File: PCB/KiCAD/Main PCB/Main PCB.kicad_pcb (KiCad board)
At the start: 2 copper layers, 118 x 118 mm, 145 parts, among them IC1 ADG608BRZ, IC2 ADG608BRZ, IC3 XB3-24Z8CM, J1 Conn_01x02, J2 Conn_01x02, J3 Conn_01x02, J4 Conn_Coaxial_Small, J5 Conn_01x02, J6 Conn_01x04, J7 Conn_01x04, J8 Conn_01x04, M1 Conn_01x02_Pin, M2 Conn_01x02_Pin, M3 Conn_01x02_Pin, M4 Conn_01x02_Pin, Q1 BSS138, Q2 BSS138, U2 Teensy4.1, U3 Teensy4.0, U4 LMD18200, U5 LMD18200, U6 LMD18200, U7 LMD18200, U8 MIC5219-3.3YM5

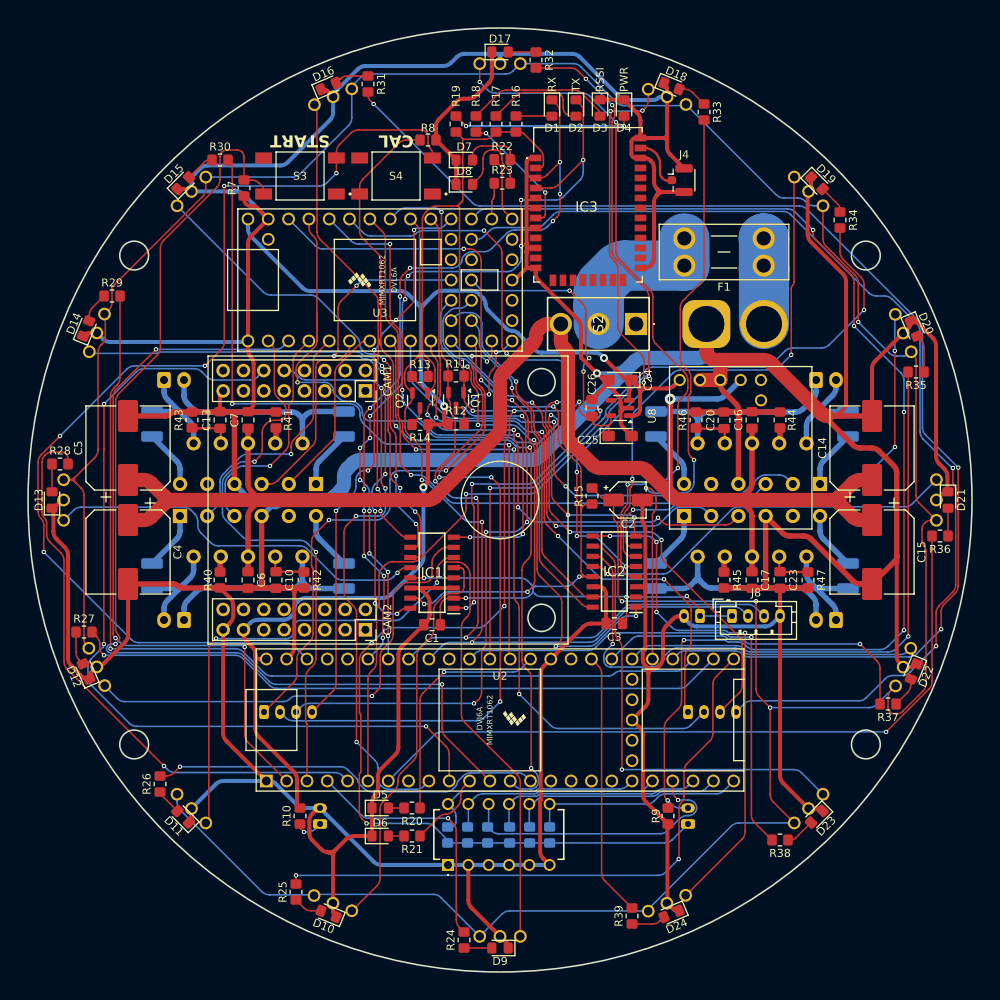
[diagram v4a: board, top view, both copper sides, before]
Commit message: New motor controllers for the main PCB
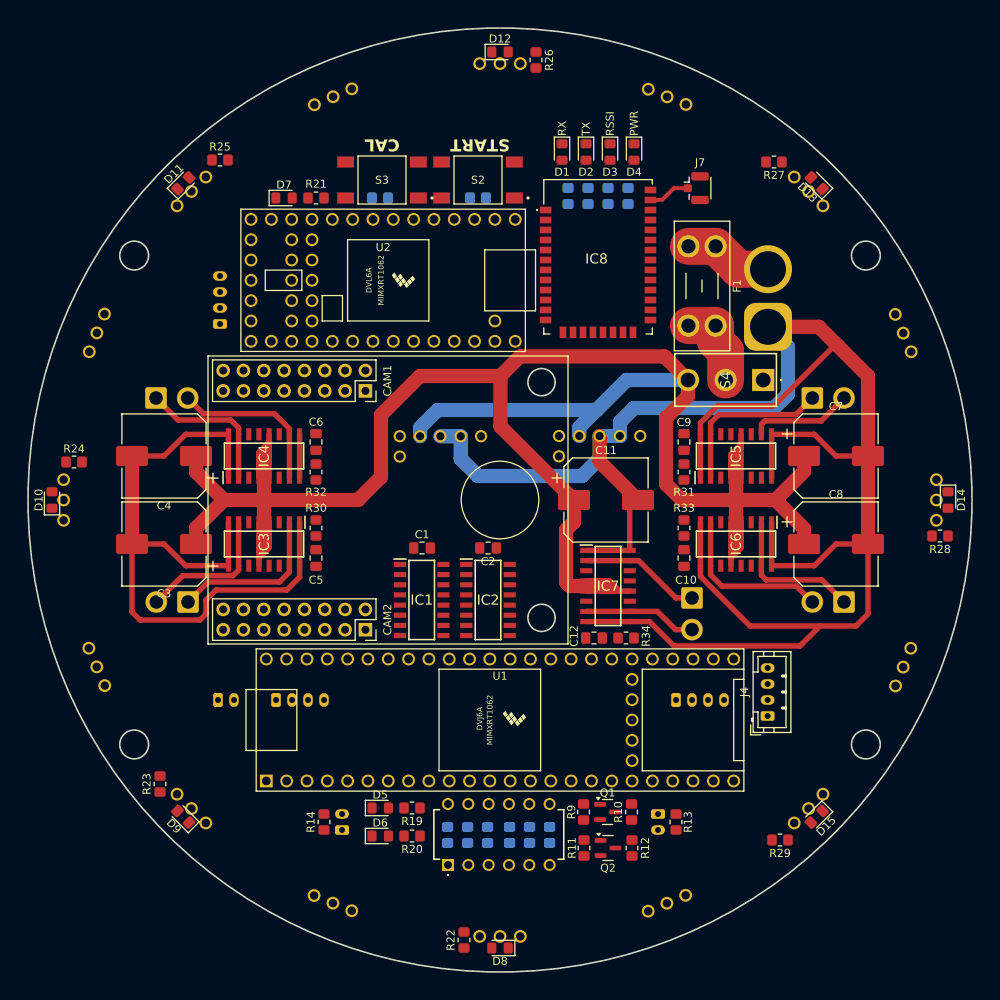
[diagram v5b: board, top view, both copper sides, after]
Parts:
- removed C13, C16, C17, C20, C23, C26: 0.1uF, Capacitor_SMD:C_0805_2012Metric_Pad1.18x1.45mm_HandSolder
- removed C14, C15: 220uF, Capacitor_SMD:CP_Elec_10x10
- removed C18, C19, C21, C22: 10nF, Capacitor_SMD:C_1210_3225Metric_Pad1.33x2.70mm_HandSolder
- removed the C2 at (16.0, 0.00)
- removed C24, C25: 10uF, Capacitor_Tantalum_SMD:CP_EIA-3216-12_Kemet-S_Pad1.58x1.35mm_HandSolder
- removed the D10 at (-21.4, 51.7)
- removed the D12 at (-51.7, 21.4)
- removed the D14 at (-51.7, -21.4)
- removed D16, D18, D20, D22, D24: BALL_DIR_LED, LED_SMD:LED_0805_2012Metric_Pad1.15x1.40mm_HandSolder
- removed the D7 at (-4.47, -42.5)
- removed the J1 at (25.8, -22.0)
- removed the J5 at (25.0, 14.5)
- removed the R15 at (11.5, -0.50)
- removed the R22 at (0.27, -42.5)
- removed the R25 at (-25.5, 49.0)
- removed the R27 at (-52.0, 16.5)
- removed the R29 at (-48.5, -25.5)
- removed R35, R37, R39: 130, Resistor_SMD:R_0805_2012Metric_Pad1.20x1.40mm_HandSolder
- removed R40, R41, R44, R45: 0, Resistor_SMD:R_0805_2012Metric_Pad1.20x1.40mm_HandSolder
- removed R43, R46, R47: 2.7k, Resistor_SMD:R_0805_2012Metric_Pad1.20x1.40mm_HandSolder
- removed the S2 at (17.0, -22.0)
- removed the U1 at (30.0, -5.88)
- removed U5, U6, U7: LMD18200, Package_TO_SOT_THT:TO-220-11_P3.4x5.08mm_StaggerOdd_Lead4.58mm_Vertical
- removed U8: MIC5219-3.3YM5, Package_TO_SOT_SMD:SOT-23-5
- added C4: 220uF, Capacitor_SMD:CP_Elec_10x10, F.Cu at (-42.0, -5.50)
- added DRIBBLER1: Conn_01x02, Connector_JST:JST_VH_B2P-VH-B_1x02_P3.96mm_Vertical, B.Cu at (24.0, 12.2)
- added IC3: VNH7070ASTR, VNH7070ASTR:SOIC127P600X175-16N, F.Cu at (-29.5, 5.50)
- added IC4: VNH7070ASTR, VNH7070ASTR:SOIC127P600X175-16N, F.Cu at (-29.5, -5.50)
- added IC5: VNH7070ASTR, VNH7070ASTR:SOIC127P600X175-16N, F.Cu at (29.5, -5.50)
- added IC6: VNH7070ASTR, VNH7070ASTR:SOIC127P600X175-16N, F.Cu at (29.5, 5.50)
- added IC7: VNH7070ASTR, VNH7070ASTR:SOIC127P600X175-16N, F.Cu at (13.5, 10.8)
- added J3: Conn_01x04, Connector_JST:JST_PH_B4B-PH-K_1x04_P2.00mm_Vertical, B.Cu at (22.0, 25.0)
- added J8: Conn_01x02, Connector_AMASS:AMASS_XT60-M_1x02_P7.20mm_Vertical, B.Cu at (33.5, -21.6)
- added J9: Conn_01x02, Connector_JST:JST_PH_B2B-PH-K_1x02_P2.00mm_Vertical, B.Cu at (-35.2, 25.0)
- added R32: 1k, Resistor_SMD:R_0805_2012Metric_Pad1.20x1.40mm_HandSolder, F.Cu at (-23.0, -3.50)
- added R34: 1k, Resistor_SMD:R_0805_2012Metric_Pad1.20x1.40mm_HandSolder, F.Cu at (15.8, 17.2)
- added S4: 1101M2S3CGE2, 1101M2S3CGE2:1101M2S3CGE2, F.Cu at (32.9, -15.0)
- added U3: ~, Pololu:D36V28F3, B.Cu at (10.0, 1.12)
- C10, C6: value 0.1uF -> 33nF
- C11, C8: value 10nF -> 220uF; footprint Capacitor_SMD:C_1210_3225Metric_Pad1.33x2.70mm_HandSolder -> Capacitor_SMD:CP_Elec_10x10; moved to F.Cu
- C12, C9: value 10nF -> 33nF; footprint Capacitor_SMD:C_1210_3225Metric_Pad1.33x2.70mm_HandSolder -> Capacitor_SMD:C_0805_2012Metric_Pad1.18x1.45mm_HandSolder; moved to F.Cu
- C5: value 220uF -> 33nF; footprint Capacitor_SMD:CP_Elec_10x10 -> Capacitor_SMD:C_0805_2012Metric_Pad1.18x1.45mm_HandSolder
- C7: value 0.1uF -> 220uF; footprint Capacitor_SMD:C_0805_2012Metric_Pad1.18x1.45mm_HandSolder -> Capacitor_SMD:CP_Elec_10x10
- M1, M2, M3, M4: value Conn_01x02_Pin -> Conn_01x02; footprint Connector_JST:JST_XH_B2B-XH-A_1x02_P2.50mm_Vertical -> Connector_JST:JST_VH_B2P-VH-B_1x02_P3.96mm_Vertical
- R15: renamed from R16; moved to B.Cu
- R16: renamed from R17; moved to B.Cu
- R17: renamed from R18; moved to B.Cu
- R18: renamed from R19; moved to B.Cu
- R3: renamed from R7; moved to B.Cu
- R30: renamed from R42; value 2.7k -> 1k
- R31, R33: value 130 -> 1k
- R4: renamed from R8; moved to B.Cu
- U4: value LMD18200 -> ~; footprint Package_TO_SOT_THT:TO-220-11_P3.4x5.08mm_StaggerOdd_Lead4.58mm_Vertical -> Pololu:D36V28F5
- moved C8 85.6 mm to (42.0, 5.50), turned to 0 degrees
- moved J2 76.0 mm to (-35.0, -22.0), turned to 90 degrees
- moved C7 73.6 mm to (42.0, -5.50), turned to 0 degrees
- moved R31 62.5 mm to (23.0, -3.50), turned to 90 degrees
- moved R11 62.4 mm to (10.5, 43.5), turned to 90 degrees
- moved C12 61.4 mm to (11.8, 17.2), turned to 180 degrees
- moved Q2 60.7 mm to (13.5, 43.5), turned to 0 degrees
- moved R12 59.2 mm to (16.5, 43.5), turned to -90 degrees
- moved R9 56.8 mm to (10.4, 39.0), turned to -90 degrees
- moved Q1 54.9 mm to (13.4, 39.0), turned to 0 degrees
- moved R10 53.2 mm to (16.4, 39.0), turned to 90 degrees
- moved R33 52.1 mm to (23.0, 3.50)
- moved C10 51.1 mm to (23.0, 7.25), turned to 90 degrees
- moved C9 45.7 mm to (23.0, -7.25)
- moved C11 34.1 mm to (13.2, 0.00), turned to 0 degrees
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- renumbered C3 to C2, C4 to C3, D13 to D10, D15 to D11, D17 to D12, D19 to D13, D21 to D14, D23 to D15, D8 to D7, D9 to D8, D11 to D9, IC3 to IC8, J6 to J1, J7 to J2, J8 to J4, J2 to J5, J3 to J6, J4 to J7, R12 to R10, R13 to R11, R14 to R12, R9 to R13, R10 to R14, R20 to R19, R21 to R20, R23 to R21, R24 to R22, R26 to R23, R28 to R24, R30 to R25, R32 to R26, R34 to R27, R36 to R28, R38 to R29, R3 to R5, R4 to R6, R5 to R7, R6 to R8, R11 to R9, S3 to S2, S4 to S3, U2 to U1, U3 to U2
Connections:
- net STATUS_GREEN_4_1 renamed STATUS_GREEN_MAIN
- net STATUS_RED_4_1 renamed STATUS_RED_MAIN
- net TEENSY_RX renamed TEENSY_1_RX
- net TEENSY_TX renamed TEENSY_1_TX
- C1 pad 1: +3V3_4_0 -> +3V3
- C10 pad 1: Net-(U4-CURRENT_SENSE_OUTPUT) -> Net-(IC6-CS)
- C11 pad 1: Net-(M2-Pin_2) -> +12V
- C11 pad 2: Net-(U5-BOOTSTRAP1) -> GND
- C12 pad 2: Net-(M2-Pin_1) -> GND
- C2 pad 1: +3V3_4_0 -> +3V3
- C5 pad 1: +12V -> Net-(IC3-CS)
- C6 pad 1: +12V -> Net-(IC4-CS)
- C8 pad 1: Net-(M1-Pin_2) -> +12V
- C8 pad 2: Net-(U4-BOOTSTRAP1) -> GND
- C9 pad 1: Net-(U4-BOOTSTRAP2) -> Net-(IC5-CS)
- C9 pad 2: Net-(M1-Pin_1) -> GND
- IC1 pad 13: +3V3_4_0 -> +3V3
- IC1 pad 2: +3V3_4_0 -> +3V3
- IC2 pad 13: +3V3_4_0 -> +3V3
- IC2 pad 2: +3V3_4_0 -> +3V3
- J4 pad 1: +3V3_4_0 -> +3V3
- M1 pad 1: Net-(M1-Pin_1) -> OUT_A_M1
- M1 pad 2: Net-(M1-Pin_2) -> OUT_B_M1
- M2 pad 1: Net-(M2-Pin_1) -> OUT_A_M2
- M2 pad 2: Net-(M2-Pin_2) -> OUT_B_M2
- M3 pad 1: Net-(M3-Pin_1) -> OUT_A_M3
- M3 pad 2: Net-(M3-Pin_2) -> OUT_B_M3
- M4 pad 1: Net-(M4-Pin_1) -> OUT_A_M4
- M4 pad 2: Net-(M4-Pin_2) -> OUT_B_M4
- R1 pad 1: +3V3 -> Net-(U1-27_A13_SCK1)
- R1 pad 2: Net-(U2-27_A13_SCK1) -> +3V3
- R2 pad 1: +3V3 -> Net-(U1-28_RX7)
- R2 pad 2: Net-(U2-28_RX7) -> +3V3
- R21 pad 1: STATUS_GREEN_4_0 -> STATUS_GREEN_TEENSY_1
- R30 pad 1: Net-(U4-CURRENT_SENSE_OUTPUT) -> Net-(IC3-CS)
- R31 pad 1: Net-(D16-A) -> Net-(IC4-CS)
- R31 pad 2: IR_DIR_157.5 -> GND
- R33 pad 1: Net-(D18-A) -> Net-(IC6-CS)
- R33 pad 2: IR_DIR_202.5 -> GND
- R5 pad 1: +3V3 -> Net-(U1-29_TX7)
- R5 pad 2: Net-(U2-29_TX7) -> +3V3
- R6 pad 1: +3V3 -> Net-(U1-30_CRX3)
- R6 pad 2: Net-(U2-30_CRX3) -> +3V3
- R7 pad 1: +3V3 -> Net-(U1-31_CTX3)
- R7 pad 2: Net-(U2-31_CTX3) -> +3V3
- R8 pad 1: +3V3 -> Net-(U1-32_OUT1B)
- R8 pad 2: Net-(U2-32_OUT1B) -> +3V3
- S1 pad B1: Net-(U2-27_A13_SCK1) -> Net-(U1-27_A13_SCK1)
- S1 pad B2: Net-(U2-28_RX7) -> Net-(U1-28_RX7)
- S1 pad B3: Net-(U2-29_TX7) -> Net-(U1-29_TX7)
- S1 pad B4: Net-(U2-30_CRX3) -> Net-(U1-30_CRX3)
- S1 pad B5: Net-(U2-31_CTX3) -> Net-(U1-31_CTX3)
- S1 pad B6: Net-(U2-32_OUT1B) -> Net-(U1-32_OUT1B)
- S2 pad 2: +3V3_4_1 -> +3V3
- S3 pad 2: +3V3_4_1 -> +3V3
- U1 pad 14: IR_DIR_45 -> PWM_M2
- U1 pad 16: unconnected-(U2-24_A10_TX6_SCL2-Pad16) -> PWM_M4
- U1 pad 17: unconnected-(U2-25_A11_RX6_SDA2-Pad17) -> IN_A_M4
- U1 pad 18: unconnected-(U2-26_A12_MOSI1-Pad18) -> IN_B_M4
- U1 pad 19: Net-(U2-27_A13_SCK1) -> Net-(U1-27_A13_SCK1)
- U1 pad 20: Net-(U2-28_RX7) -> Net-(U1-28_RX7)
- U1 pad 21: Net-(U2-29_TX7) -> Net-(U1-29_TX7)
- U1 pad 22: Net-(U2-30_CRX3) -> Net-(U1-30_CRX3)
- U1 pad 23: Net-(U2-31_CTX3) -> Net-(U1-31_CTX3)
- U1 pad 24: Net-(U2-32_OUT1B) -> Net-(U1-32_OUT1B)
- U1 pad 25: IR_DIR_22.5 -> IR_DIR_0
- U1 pad 26: IR_DIR_67.5 -> IR_DIR_90
- U1 pad 27: IR_DIR_112.5 -> IR_DIR_180
- U1 pad 28: IR_DIR_157.5 -> IR_DIR_270
- U1 pad 29: IR_DIR_202.5 -> IR_DIR_45
- U1 pad 30: IR_DIR_247.5 -> IR_DIR_135
- U1 pad 31: IR_DIR_292.5 -> IR_DIR_225
- U1 pad 32: IR_DIR_337.5 -> IR_DIR_315
- U1 pad 36: IR_DIR_135 -> unconnected-(U1-14_A0_TX3_SPDIF_OUT-Pad36)
- U1 pad 37: IR_DIR_225 -> unconnected-(U1-15_A1_RX3_SPDIF_IN-Pad37)
- U1 pad 38: IR_DIR_315 -> COM_RX
- U1 pad 39: unconnected-(U2-17_A3_TX4_SDA1-Pad39) -> COM_TX
- U1 pad 4: IR_DIR_0 -> PWM_M1
- U1 pad 42: COM_TX -> LG_RECEIVE
- U1 pad 43: COM_RX -> IN_B_M3
- U1 pad 44: unconnected-(U2-22_A8_CTX1-Pad44) -> IN_A_M3
- U1 pad 45: unconnected-(U2-23_A9_CRX1_MCLK1-Pad45) -> PWM_M3
- U1 pad 46: +3V3_4_1 -> unconnected-(U1-3V3-Pad46)
- U1 pad 5: IR_DIR_90 -> IN_A_M1
- U1 pad 6: IR_DIR_180 -> IN_B_M1
- U1 pad 7: IR_DIR_270 -> IN_A_M2
- U1 pad 8: unconnected-(U2-6_OUT1D-Pad8) -> IN_B_M2
- U2 pad 10: MOTOR_4_SPEED -> LED_3_A0
- U2 pad 11: MOTOR_4_DIR -> LED_3_A1
- U2 pad 12: LED_1_OUT -> LED_3_A2
- U2 pad 13: LED_1_A0 -> TSSP_1_A0
- U2 pad 14: LED_1_A1 -> TSSP_1_A1
- U2 pad 20: STATUS_RED_4_0 -> STATUS_RED_TEENSY_1
- U2 pad 21: STATUS_GREEN_4_0 -> LED_1_OUT
- U2 pad 22: LG_RECEIVE -> LED_2_OUT
- U2 pad 23: LED_1_A2 -> LED_3_OUT
- U2 pad 24: LED_2_OUT -> TSSP_1_OUT
- U2 pad 27: LED_2_A0 -> TSSP_2_OUT
- U2 pad 28: LED_2_A1 -> TSSP_1_A2
- U2 pad 29: TSSP_1_OUT -> TSSP_2_A0
- U2 pad 30: TSSP_2_OUT -> TSSP_2_A1
- U2 pad 31: +3V3_4_0 -> unconnected-(U2-3V3-Pad31)
- U2 pad 35: LED_2_A2 -> unconnected-(U2-24_A10_TX6_SCL2-Pad35)
- U2 pad 37: unconnected-(U3-26_A12_MOSI1-Pad37) -> TSSP_2_A2
- U2 pad 39: TSSP_1_A0 -> unconnected-(U2-28_RX7-Pad39)
- U2 pad 4: MOTOR_1_SPEED -> LED_1_A0
- U2 pad 40: TSSP_1_A1 -> unconnected-(U2-29_TX7-Pad40)
- U2 pad 41: TSSP_1_A2 -> unconnected-(U2-30_CRX3-Pad41)
- U2 pad 42: TSSP_2_A0 -> unconnected-(U2-31_CTX3-Pad42)
- U2 pad 43: TSSP_2_A1 -> unconnected-(U2-32_OUT1B-Pad43)
- U2 pad 44: TSSP_2_A2 -> unconnected-(U2-33_MCLK2-Pad44)
- U2 pad 5: MOTOR_1_DIR -> LED_1_A1
- U2 pad 6: MOTOR_2_SPEED -> LED_1_A2
- U2 pad 7: MOTOR_2_DIR -> LED_2_A0
- U2 pad 8: MOTOR_3_SPEED -> LED_2_A1
- U2 pad 9: MOTOR_3_DIR -> LED_2_A2
- U4 pad 1: Net-(U4-BOOTSTRAP1) -> unconnected-(U4-PG-Pad1)
- U4 pad 2: Net-(M1-Pin_2) -> unconnected-(U4-EN-Pad2)
- U4 pad 3: MOTOR_1_DIR -> +12V
- U4 pad 4: MOTOR_1_BRAKE -> GND
- U4 pad 5: MOTOR_1_SPEED -> GND
- U4 pad 6: +12V -> +5V
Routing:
- net GND: track 975.3 -> 351.7 mm, vias 1 -> 0
- net TSSP_PWR: track 410.6 -> 0.00 mm, vias 4 -> 0
- net +3V3: track 214.7 -> 0.00 mm, vias 6 -> 0
- net +5V: track 165.9 -> 0.00 mm, vias 3 -> 0
- net IR_DIR_157.5: track 157.6 -> 0.00 mm, vias 3 -> 0
- net LG_RECEIVE: track 152.4 -> 0.00 mm, vias 6 -> 0
- net +3V3_4_0: track 148.1 -> 0.00 mm, vias 8 -> 0
- net START_BUTTON: track 136.4 -> 0.00 mm, vias 2 -> 0
- net +12V: track 201.0 -> 334.7 mm, vias 1 -> 0
- net LED_2_A2: track 133.7 -> 0.00 mm, vias 2 -> 0
- net +3V3_4_1: track 132.5 -> 0.00 mm, vias 5 -> 0
- net IR_DIR_112.5: track 119.3 -> 0.00 mm, vias 1 -> 0
- net IR_DIR_180: track 119.1 -> 0.00 mm, vias 4 -> 0
- net 3V3_SCL: track 113.6 -> 0.00 mm, vias 4 -> 0
- net CAMERA_TX: track 110.5 -> 0.00 mm, vias 3 -> 0
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
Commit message: Added a dribbler motor controller
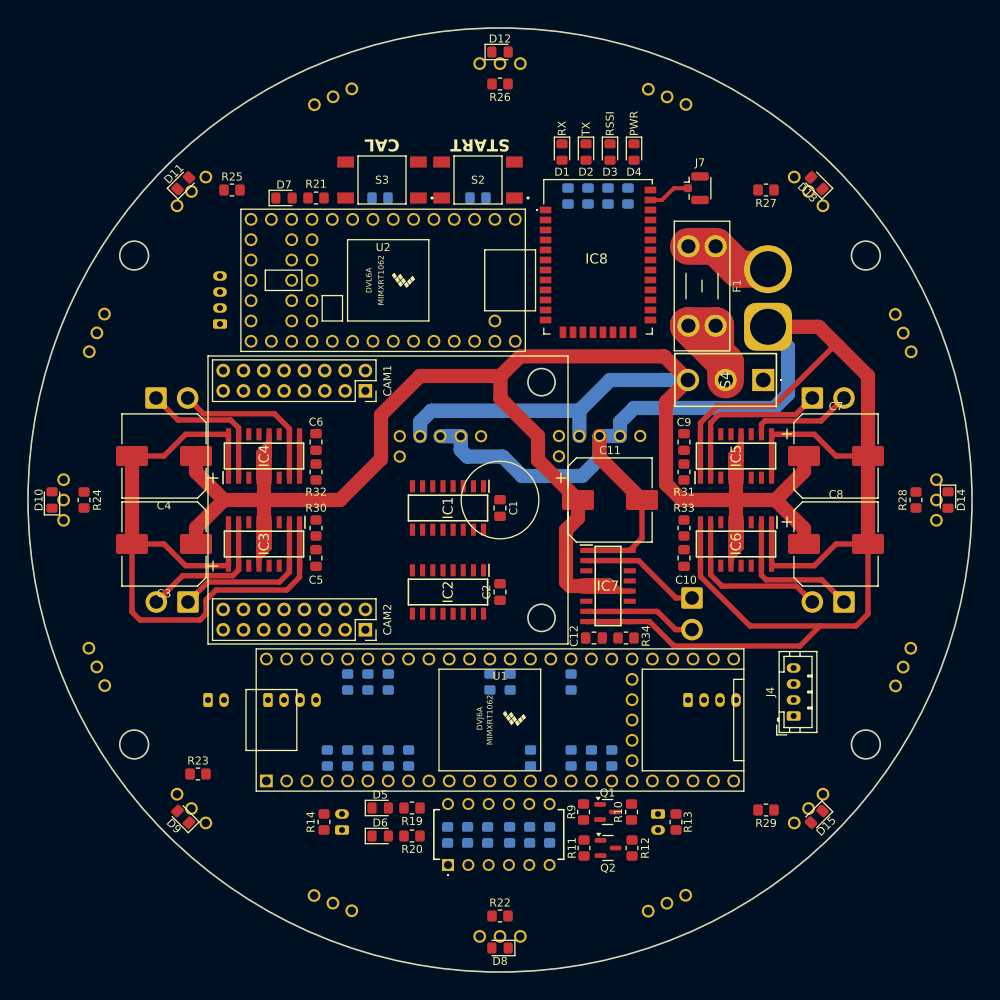
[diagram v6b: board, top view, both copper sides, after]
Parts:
- added R35: 1k, Resistor_SMD:R_0805_2012Metric_Pad1.20x1.40mm_HandSolder, B.Cu at (-21.6, 32.2)
- added R36: 1k, Resistor_SMD:R_0805_2012Metric_Pad1.20x1.40mm_HandSolder, B.Cu at (-19.1, 32.2)
- added R37: 1k, Resistor_SMD:R_0805_2012Metric_Pad1.20x1.40mm_HandSolder, B.Cu at (-16.5, 32.2)
- added R38: 1k, Resistor_SMD:R_0805_2012Metric_Pad1.20x1.40mm_HandSolder, B.Cu at (-14.0, 32.2)
- added R39: 1k, Resistor_SMD:R_0805_2012Metric_Pad1.20x1.40mm_HandSolder, B.Cu at (-11.4, 32.2)
- added R40: 1k, Resistor_SMD:R_0805_2012Metric_Pad1.20x1.40mm_HandSolder, B.Cu at (8.89, 32.2)
- added R41: 1k, Resistor_SMD:R_0805_2012Metric_Pad1.20x1.40mm_HandSolder, B.Cu at (14.0, 32.2)
- added R42: 1k, Resistor_SMD:R_0805_2012Metric_Pad1.20x1.40mm_HandSolder, B.Cu at (11.4, 32.2)
- added R43: 1k, Resistor_SMD:R_0805_2012Metric_Pad1.20x1.40mm_HandSolder, B.Cu at (3.81, 32.2)
- added R44: 1k, Resistor_SMD:R_0805_2012Metric_Pad1.20x1.40mm_HandSolder, B.Cu at (-19.1, 22.8)
- added R45: 1k, Resistor_SMD:R_0805_2012Metric_Pad1.20x1.40mm_HandSolder, B.Cu at (-14.0, 22.8)
- added R46: 1k, Resistor_SMD:R_0805_2012Metric_Pad1.20x1.40mm_HandSolder, B.Cu at (-16.5, 22.8)
- added R47: 1k, Resistor_SMD:R_0805_2012Metric_Pad1.20x1.40mm_HandSolder, B.Cu at (-1.27, 22.8)
- added R48: 1k, Resistor_SMD:R_0805_2012Metric_Pad1.20x1.40mm_HandSolder, B.Cu at (8.89, 22.8)
- added R49: 1k, Resistor_SMD:R_0805_2012Metric_Pad1.20x1.40mm_HandSolder, B.Cu at (1.27, 22.8)
- moved IC1 12.0 mm to (-6.50, 1.00), turned to -90 degrees
- moved C1 11.0 mm to (0.00, 1.00), turned to -90 degrees
- moved C2 5.70 mm to (0.00, 11.5), turned to 90 degrees
- moved R22 5.41 mm to (0.00, 52.0), turned to 0 degrees
- moved R26 5.41 mm to (0.00, -52.0), turned to 180 degrees
- moved R28 5.41 mm to (52.0, 0.00), turned to 90 degrees
- moved IC2 5.10 mm to (-6.50, 11.5), turned to -90 degrees
- moved R23 4.91 mm to (-37.8, 34.2), turned to 0 degrees
- moved R24 4.91 mm to (-52.0, 0.00), turned to -90 degrees
- moved R29 4.14 mm to (33.2, 38.8)
- moved R25 4.04 mm to (-33.5, -38.8)
- moved R27 3.64 mm to (33.2, -38.8)
- moved J4 3.25 mm to (36.7, 27.0)
- moved J3 1.50 mm to (23.5, 25.0)
- moved J9 1.25 mm to (-36.5, 25.0)
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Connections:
- U1 pad 14: PWM_M2 -> Net-(U1-12_MISO_MQSL)
- U1 pad 16: PWM_M4 -> Net-(U1-24_A10_TX6_SCL2)
- U1 pad 17: IN_A_M4 -> Net-(U1-25_A11_RX6_SDA2)
- U1 pad 18: IN_B_M4 -> Net-(U1-26_A12_MOSI1)
- U1 pad 33: unconnected-(U1-41_A17-Pad33) -> Net-(U1-41_A17)
- U1 pad 36: unconnected-(U1-14_A0_TX3_SPDIF_OUT-Pad36) -> Net-(U1-14_A0_TX3_SPDIF_OUT)
- U1 pad 37: unconnected-(U1-15_A1_RX3_SPDIF_IN-Pad37) -> Net-(U1-15_A1_RX3_SPDIF_IN)
- U1 pad 4: PWM_M1 -> Net-(U1-2_OUT2)
- U1 pad 43: IN_B_M3 -> Net-(U1-21_A7_RX5_BCLK1)
- U1 pad 44: IN_A_M3 -> Net-(U1-22_A8_CTX1)
- U1 pad 45: PWM_M3 -> Net-(U1-23_A9_CRX1_MCLK1)
- U1 pad 5: IN_A_M1 -> Net-(U1-3_LRCLK2)
- U1 pad 6: IN_B_M1 -> Net-(U1-4_BCLK2)
- U1 pad 7: IN_A_M2 -> Net-(U1-5_IN2)
- U1 pad 8: IN_B_M2 -> Net-(U1-6_OUT1D)
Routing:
- net Net-(S4-COM): track 10.7 -> 22.1 mm
- net +12V: track 334.7 -> 327.9 mm
